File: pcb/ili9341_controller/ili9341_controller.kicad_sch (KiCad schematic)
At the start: 33 parts, among them U1 ICE40HX1K-VQ100, U2 RP2040

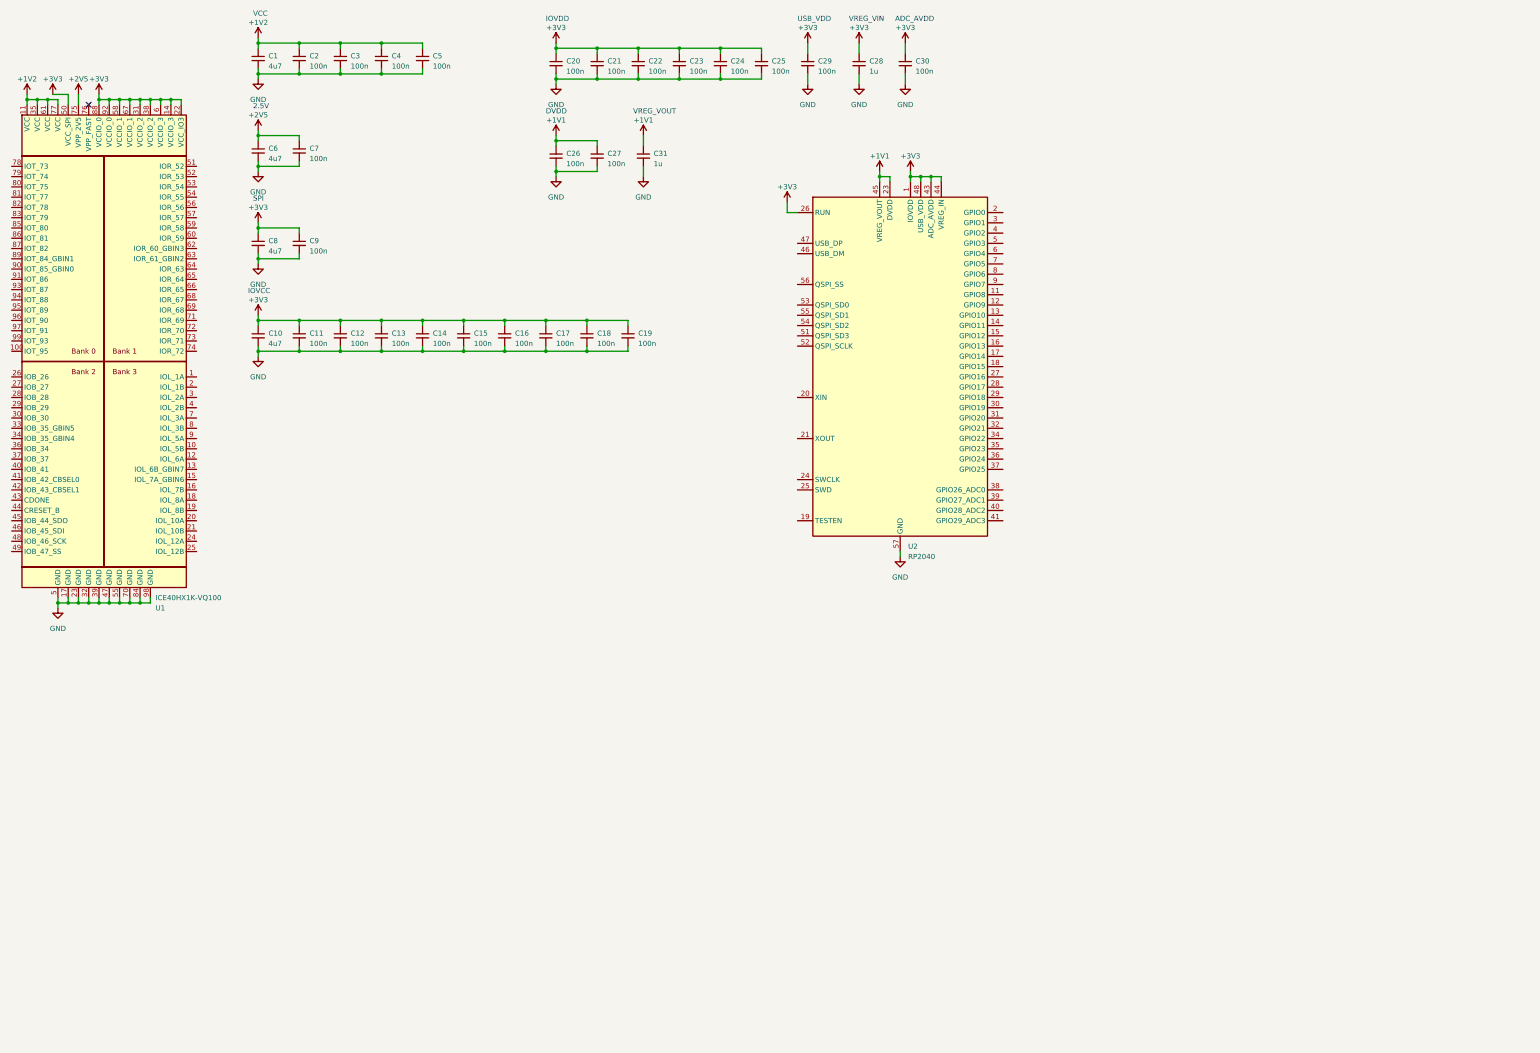
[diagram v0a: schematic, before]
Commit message: update pcb, begin adding in support for lattice fpga
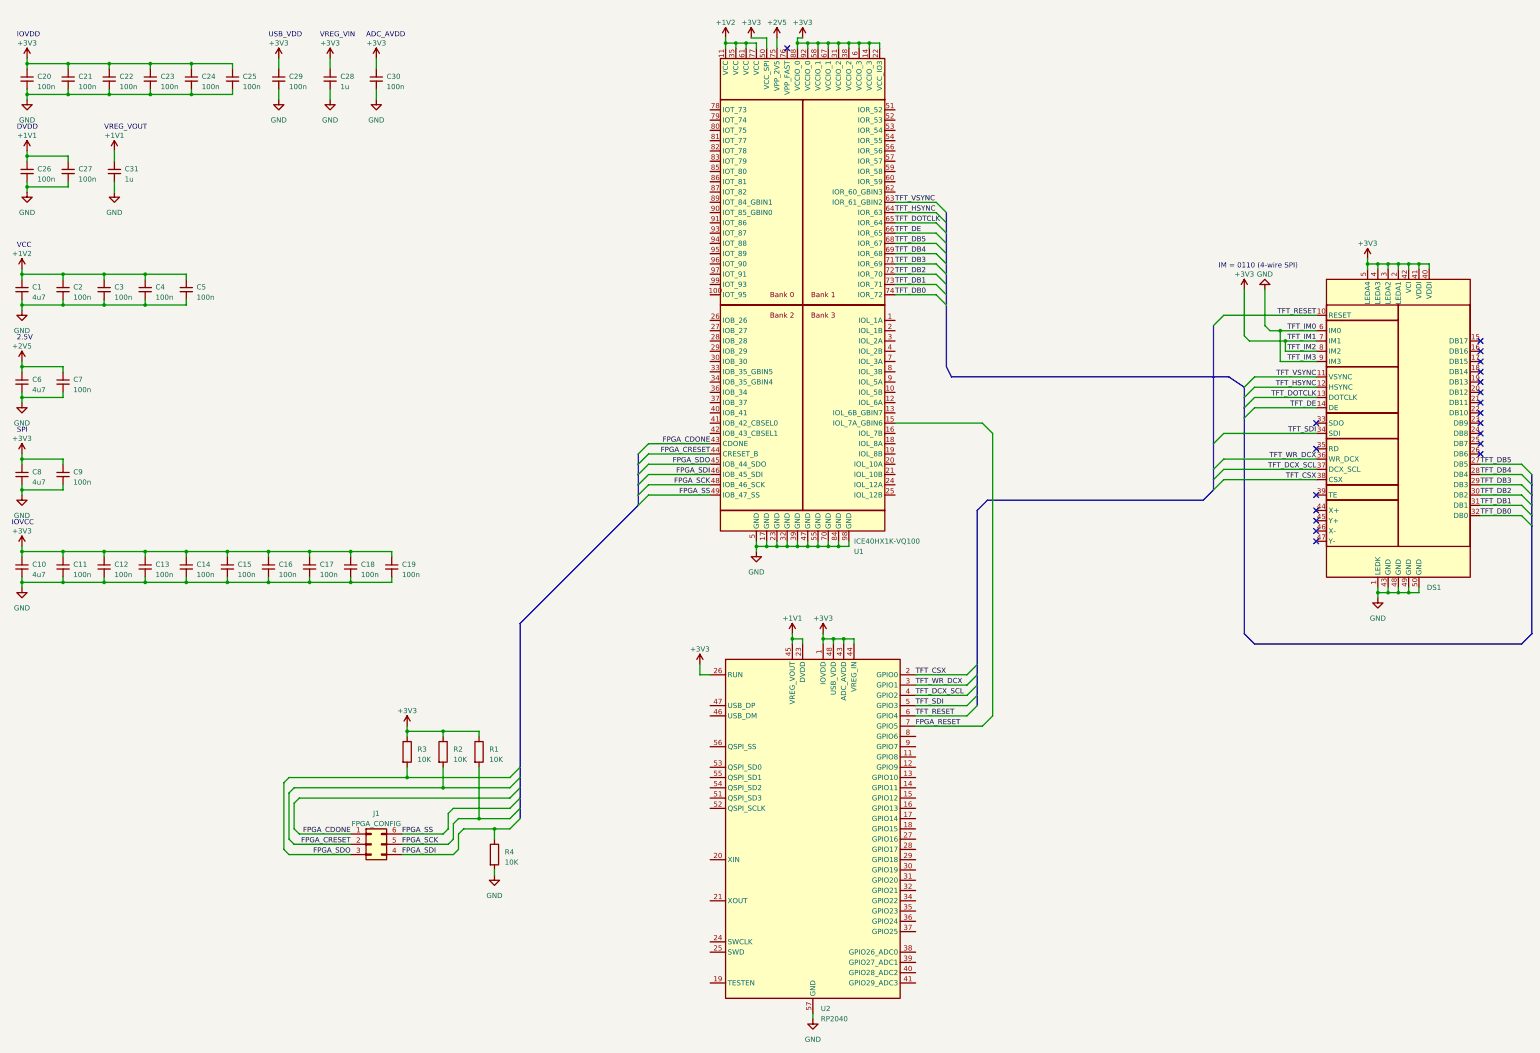
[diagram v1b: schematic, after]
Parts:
- added DS1: ~, Connector_FFC-FPC:Molex_54132-5033_1x50-1MP_P0.5mm_Horizontal, symbol MI0283QT-11:MI0283QT-11
- added J1: FPGA_CONFIG, Connector_PinHeader_2.54mm:PinHeader_2x03_P2.54mm_Vertical, symbol Connector_Generic:Conn_02x03_Counter_Clockwise
- added R1, R2, R3, R4: 10K, symbol Device:R
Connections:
- net +3V3: now also DS1.2 (LEDA1), DS1.3 (LEDA2), DS1.4 (LEDA3), DS1.40 (VDDI), DS1.41 (VDDI), DS1.42 (VCI), DS1.5 (LEDA4), DS1.7 (IM1), DS1.8 (IM2), R1.1, R2.1, R3.1
- net GND: now also DS1.1 (LEDK), DS1.43 (GND), DS1.48 (GND), DS1.49 (GND), DS1.50 (GND), DS1.6 (IM0), DS1.9 (IM3), R4.2
- net TFT_CSX: now reaches U2.2 (GPIO0)
- net TFT_CSX: now also DS1.38 (CSX)
- net TFT_WR_DCX: now reaches U2.3 (GPIO1)
- net TFT_WR_DCX: now also DS1.36 (WR_DCX)
- net TFT_DCX_SCL: now reaches U2.4 (GPIO2)
- net TFT_DCX_SCL: now also DS1.37 (DCX_SCL)
- net TFT_SDI: now reaches U2.5 (GPIO3)
- net TFT_SDI: now also DS1.34 (SDI)
- net TFT_RESET: now reaches U2.6 (GPIO4)
- net TFT_RESET: now also DS1.10 (RESET)
- net FPGA_RESET: now reaches U2.7 (GPIO5)
- net FPGA_RESET: now also U1.15 (IOL_7A_GBIN6)
- net FPGA_CDONE: now reaches U1.43 (CDONE)
- net FPGA_CDONE: now also J1.1 (Pin_1)
- net FPGA_CRESET: now reaches U1.44 (CRESET_B)
- net FPGA_CRESET: now also J1.2 (Pin_2), R2.2
- net FPGA_SDO: now reaches U1.45 (IOB_44_SDO)
- net FPGA_SDO: now also J1.3 (Pin_3), R3.2
- net FPGA_SDI: now reaches U1.46 (IOB_45_SDI)
- net FPGA_SDI: now also J1.4 (Pin_4), R4.1
- net FPGA_SCK: now reaches U1.48 (IOB_46_SCK)
- net FPGA_SCK: now also J1.5 (Pin_5), R1.2
- net FPGA_SS: now reaches U1.49 (IOB_47_SS)
- net FPGA_SS: now also J1.6 (Pin_6)
- net TFT_VSYNC: now reaches U1.63 (IOR_61_GBIN2)
- net TFT_VSYNC: now also DS1.11 (VSYNC)
- net TFT_HSYNC: now reaches U1.64 (IOR_63)
- net TFT_HSYNC: now also DS1.12 (HSYNC)
- net TFT_DOTCLK: now reaches U1.65 (IOR_64)
- net TFT_DOTCLK: now also DS1.13 (DOTCLK)
- net TFT_DE: now reaches U1.66 (IOR_65)
- net TFT_DE: now also DS1.14 (DE)
- net TFT_DB5: now reaches U1.68 (IOR_67)
- net TFT_DB5: now also DS1.27 (DB5)
- net TFT_DB4: now reaches U1.69 (IOR_68)
- net TFT_DB4: now also DS1.28 (DB4)
- net TFT_DB3: now reaches U1.71 (IOR_69)
- net TFT_DB3: now also DS1.29 (DB3)
- net TFT_DB2: now reaches U1.72 (IOR_70)
- net TFT_DB2: now also DS1.30 (DB2)
- net TFT_DB1: now reaches U1.73 (IOR_71)
- net TFT_DB1: now also DS1.31 (DB1)
- net TFT_DB0: now reaches U1.74 (IOR_72)
- net TFT_DB0: now also DS1.32 (DB0)
- no-connect marks 1 -> 20
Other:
- note added: "IM = 0110 (4-wire SPI)"
- moved on the sheet: C1, C10, C11, C12, C13, C14, C15, C16, C17, C18, C19, C2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
